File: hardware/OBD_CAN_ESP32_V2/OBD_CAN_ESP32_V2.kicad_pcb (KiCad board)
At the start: 2 copper layers, 66 x 36 mm, 20 parts, among them J3 ESP32_S3_DEVKITC_J1, J4 ESP32_S3_DEVKITC_J3, Q1 Q_PMOS_GDS, U1 SN65HVD230

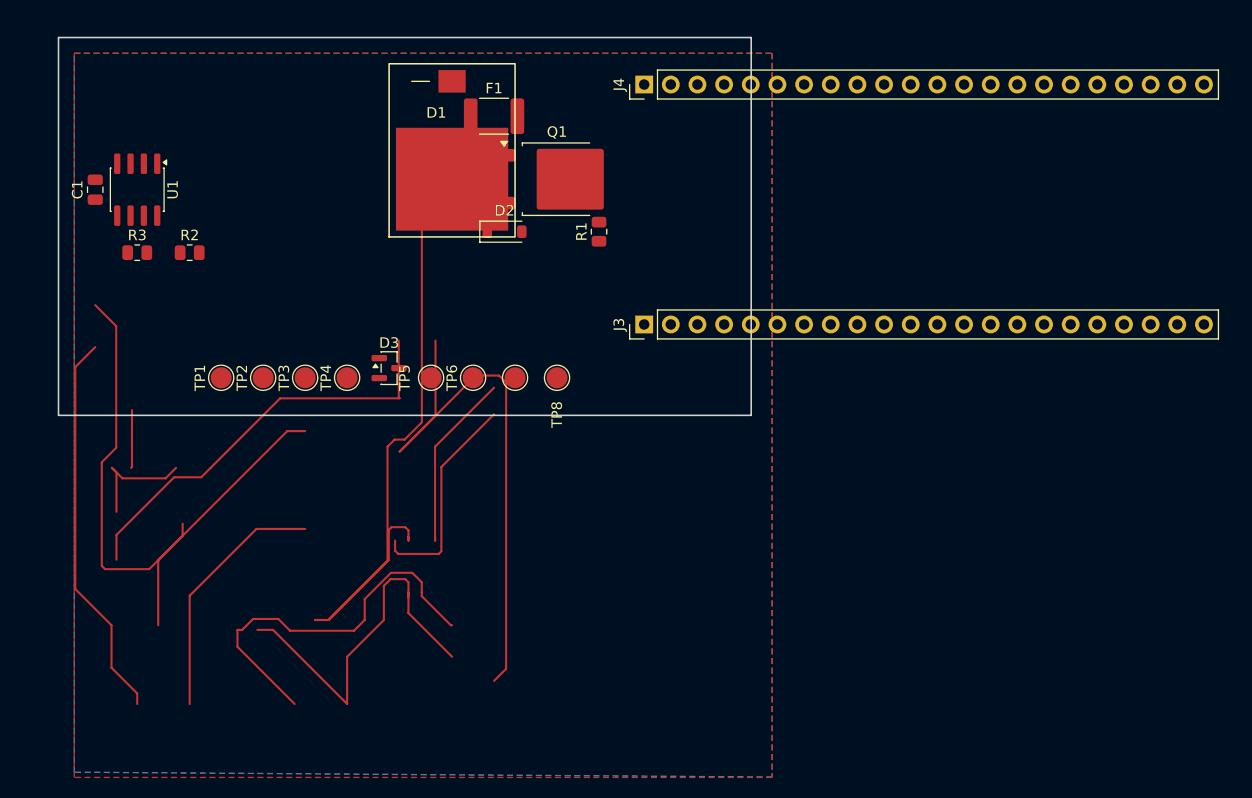
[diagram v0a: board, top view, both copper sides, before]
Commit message: hardware: V2 재작성 — 기존 라우팅/존 정리, 헤더 원점 수정
- V1의 트랙 97개 삭제(재배치로 무효), 구리 존 2개는 새 외곽으로 재정의
- 데브킷 헤더 원점을 좌측(61mm)으로 — 핀이 보드 안쪽으로 뻗도록
- 별도 폴더 OBD_CAN_ESP32_V2로 분리

Co-Authored-By: Claude Fable 5 <noreply@anthropic.com>
Claude-Session: https://claude.ai/code/session_015Lj2iN8K2AKiUuQKmtXaeP
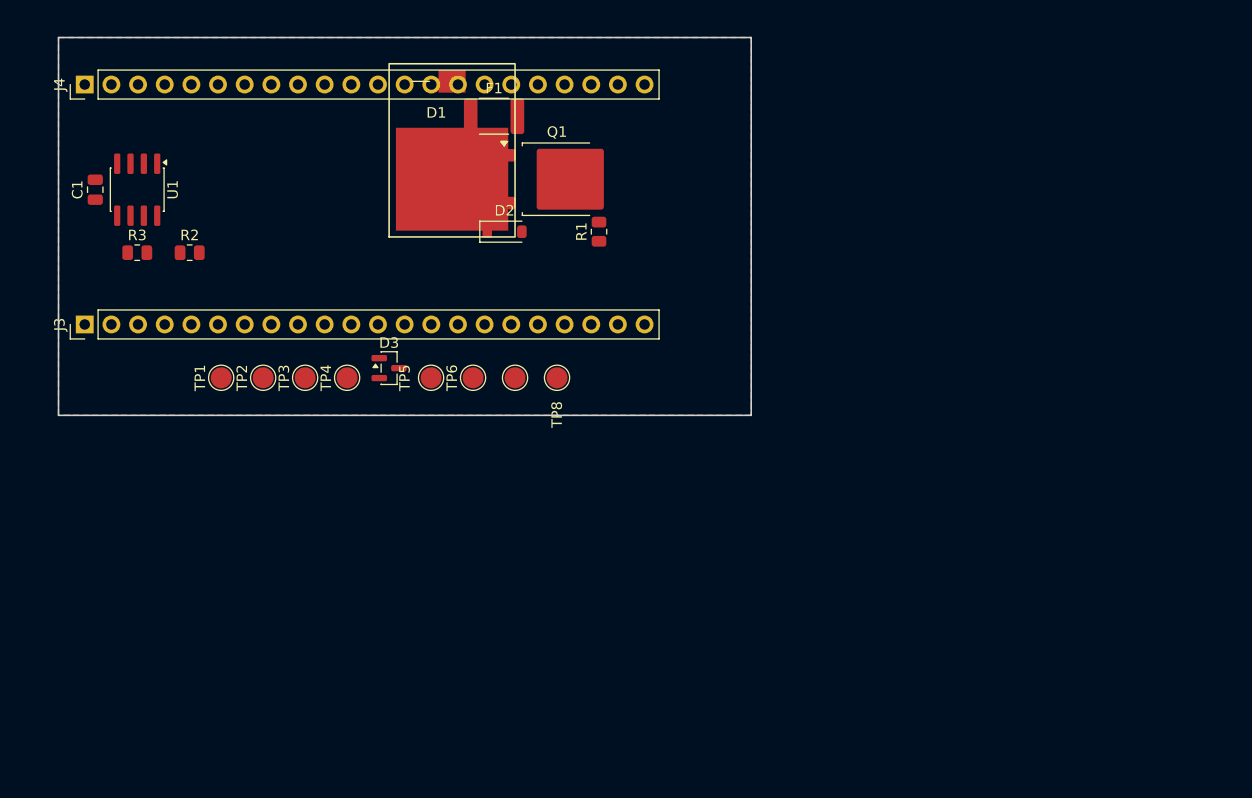
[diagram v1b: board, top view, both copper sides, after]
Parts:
- moved J3 53.3 mm to (61.0, 116.8)
- moved J4 53.3 mm to (61.0, 94.0)
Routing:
- net /+3V3: track 74.5 -> 0.00 mm
- net /VBAT_FUSED: track 61.8 -> 0.00 mm
- net /+5V: track 54.3 -> 0.00 mm
- net /VBAT_PROTECTED: track 40.3 -> 0.00 mm
- net /VBAT_OBD: track 37.2 -> 0.00 mm
- net /CAN_H: track 37.0 -> 0.00 mm
- net /CAN_L: track 36.2 -> 0.00 mm
- net /CHASSIS_GND: track 23.9 -> 0.00 mm
- net /CAN_RX: track 20.7 -> 0.00 mm
- net /CAN_TX: track 17.2 -> 0.00 mm
- net Net-(D2-K): track 11.3 -> 0.00 mm
- net /SIGNAL_GND: track 5.54 -> 0.00 mm

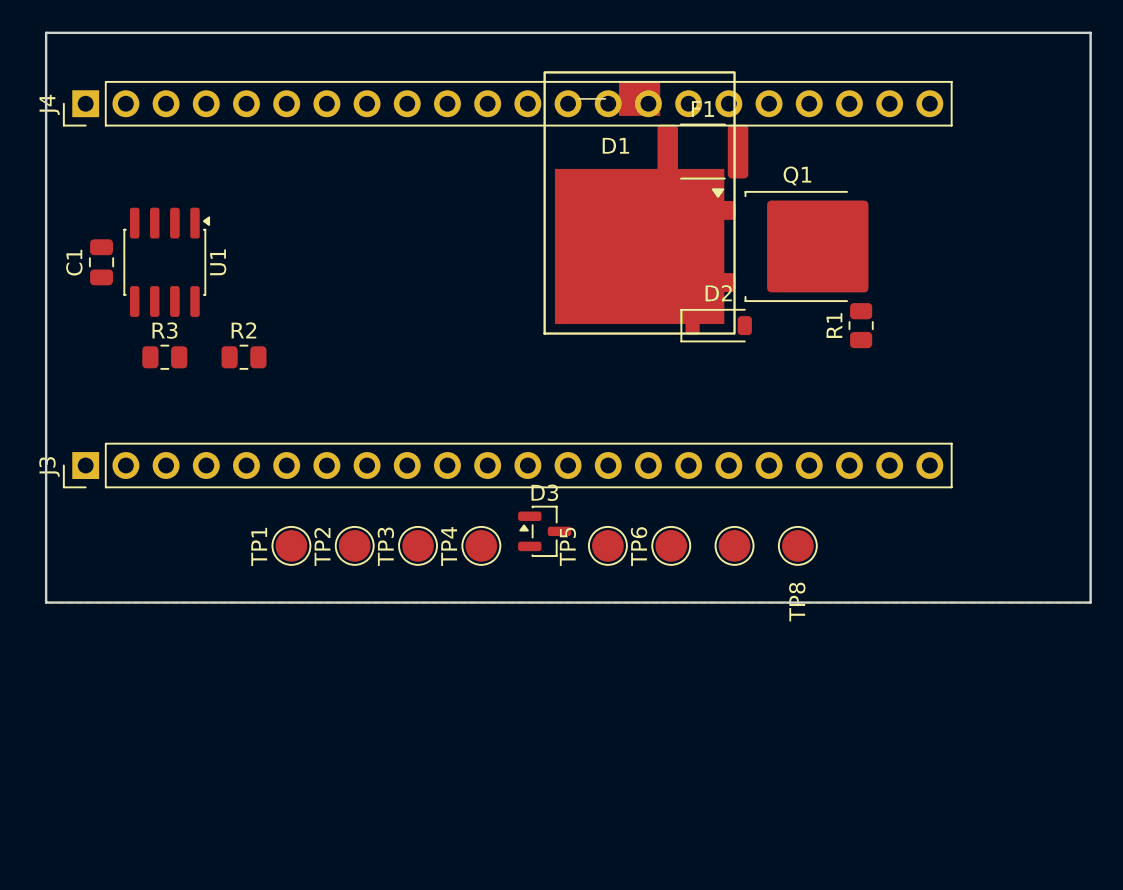
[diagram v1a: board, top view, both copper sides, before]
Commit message: hardware: V2 PCB 66x44 부품 배치 완료 (옵션2, 겹침 0 검증)
- 보드 66x36 → 66x44 (D1 SM8S24A 대형 TVS 수용)
- 존 배치: CAN(좌)/벅(중앙)/입력보호(하단)/커넥터+TP(최하단)
- 자체 커트야드 겹침 검사 통과 (겹침 0, 외곽 초과 0)

Co-Authored-By: Claude Fable 5 <noreply@anthropic.com>
Claude-Session: https://claude.ai/code/session_015Lj2iN8K2AKiUuQKmtXaeP
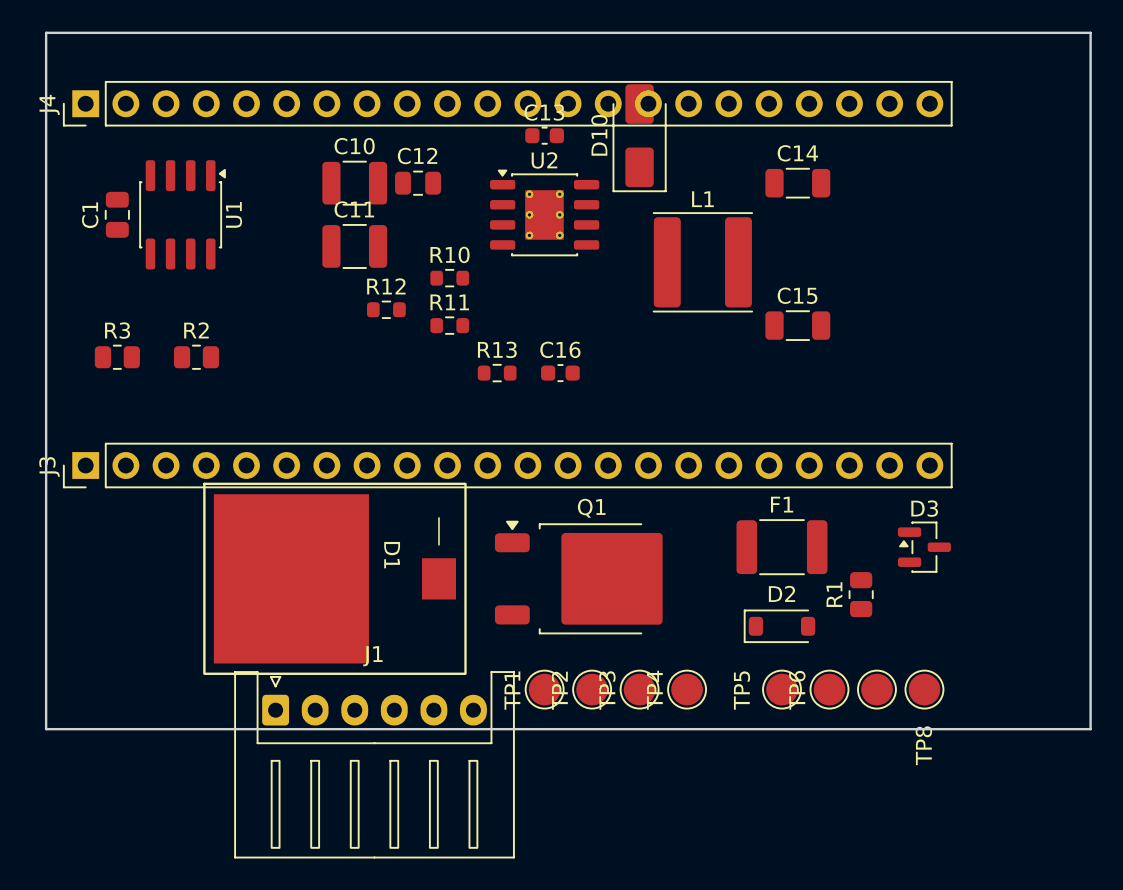
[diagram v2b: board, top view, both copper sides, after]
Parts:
- added C10: 2.2µF/100V, Capacitor_SMD:C_1210_3225Metric, F.Cu at (78.0, 99.0)
- added C11: 2.2µF/100V, Capacitor_SMD:C_1210_3225Metric, F.Cu at (78.0, 103.0)
- added C12: 100nF/100V, Capacitor_SMD:C_0805_2012Metric, F.Cu at (82.0, 99.0)
- added C13: 100nF, Capacitor_SMD:C_0603_1608Metric, F.Cu at (90.0, 96.0)
- added C14: 22µF/16V, Capacitor_SMD:C_1206_3216Metric, F.Cu at (106.0, 99.0)
- added C15: 22µF/16V, Capacitor_SMD:C_1206_3216Metric, F.Cu at (106.0, 108.0)
- added C16: 3300pF, Capacitor_SMD:C_0603_1608Metric, F.Cu at (91.0, 111.0)
- added D10: B360A, Diode_SMD:D_SMA, F.Cu at (96.0, 96.0)
- added J1: OBD-II INPUT, Connector_JST:JST_XH_S6B-XH-A_1x06_P2.50mm_Horizontal, F.Cu at (73.0, 132.3)
- added L1: 10µH 4A, Inductor_SMD:L_Sunlord_SWPA6045S, F.Cu at (100.0, 104.0)
- added R10: 52.3kΩ 1%, Resistor_SMD:R_0603_1608Metric, F.Cu at (84.0, 105.0)
- added R11: 10kΩ 1%, Resistor_SMD:R_0603_1608Metric, F.Cu at (84.0, 108.0)
- added R12: 182kΩ 1%, Resistor_SMD:R_0603_1608Metric, F.Cu at (80.0, 107.0)
- added R13: 8.06kΩ, Resistor_SMD:R_0603_1608Metric, F.Cu at (87.0, 111.0)
- added U2: TPS54360BDDA, Package_SO:HSOP-8-1EP_3.9x4.9mm_P1.27mm_EP2.41x3.1mm_ThermalVias, F.Cu at (90.0, 101.0)
- moved D1 30.4 mm to (74.0, 124.0), turned to 0 degrees
- moved F1 25.5 mm to (105.0, 122.0)
- moved Q1 24.7 mm to (93.0, 124.0)
- moved D3 24.0 mm to (114.0, 122.0)
- moved D2 19.4 mm to (105.0, 127.0)
- moved TP1 18.4 mm to (90.0, 131.0)
- moved TP2 17.5 mm to (93.0, 131.0)
- moved R1 17.0 mm to (110.0, 125.0)
- moved TP3 16.7 mm to (96.0, 131.0)
- moved TP4 15.9 mm to (99.0, 131.0)
- moved TP5 14.3 mm to (105.0, 131.0)
- moved TP6 13.5 mm to (108.0, 131.0)
- moved TP7 12.8 mm to (111.0, 131.0)
- moved TP8 12.1 mm to (114.0, 131.0)
- moved C1 3.16 mm to (63.0, 101.0)
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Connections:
- D2 pad 1: Net-(D2-K) -> /VBAT_PROTECTED
- D2 pad 2: /VBAT_PROTECTED -> Net-(D2-A)
- Q1 pad 1: Net-(D2-K) -> Net-(D2-A)
- R1 pad 1: Net-(D2-K) -> Net-(D2-A)
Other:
- board size 66 x 36 mm -> 66 x 44 mm

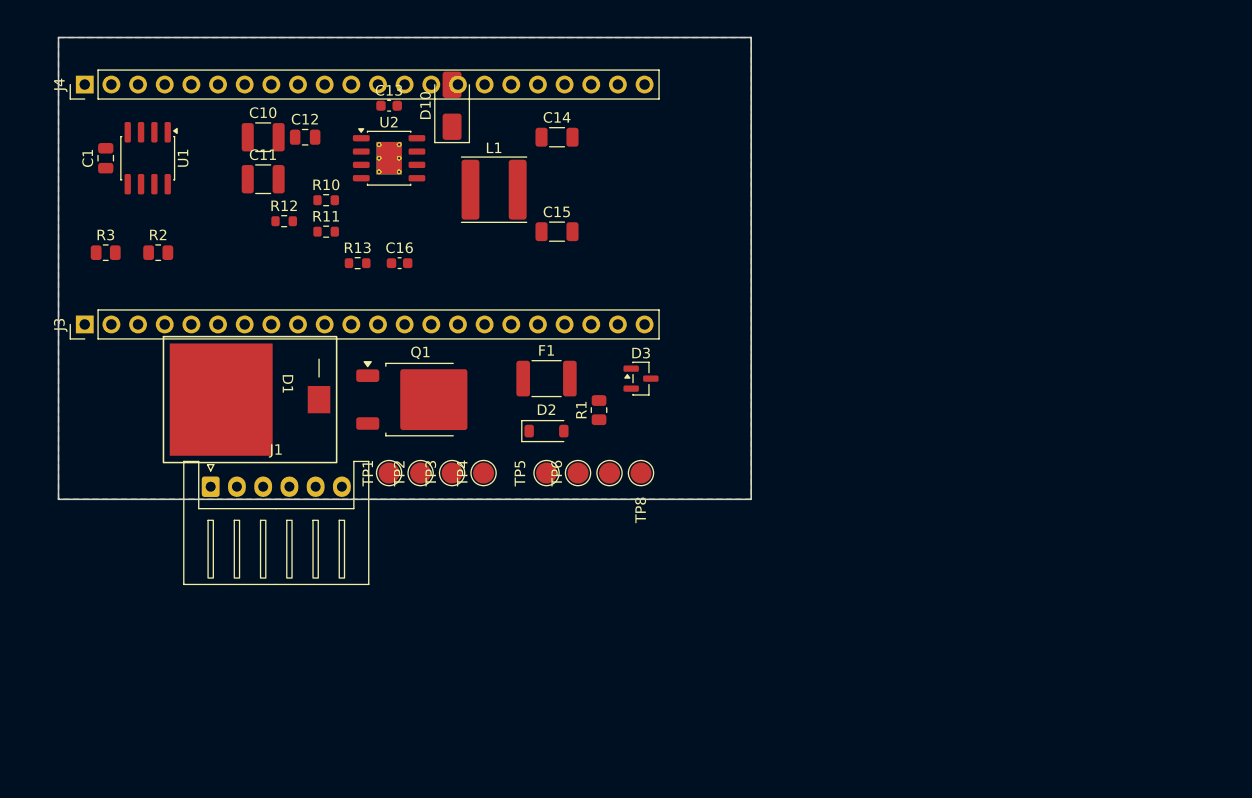
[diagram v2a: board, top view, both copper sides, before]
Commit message: hardware: V2 66x36 양면 배치 + M2.5 나사구멍 4개
- 보드 66x44 → 66x36 복원 (D1/Q1 뒷면 이설 전제)
- 앞면 부품 재배치, 겹침 0 검증
- 네 모서리 M2.5 마운팅홀(H1~H4) 추가 (케이스 고정용)
- D1/Q1은 뒷면 전환 대기 (사용자가 KiCad F키로 전환)

Co-Authored-By: Claude Fable 5 <noreply@anthropic.com>
Claude-Session: https://claude.ai/code/session_015Lj2iN8K2AKiUuQKmtXaeP
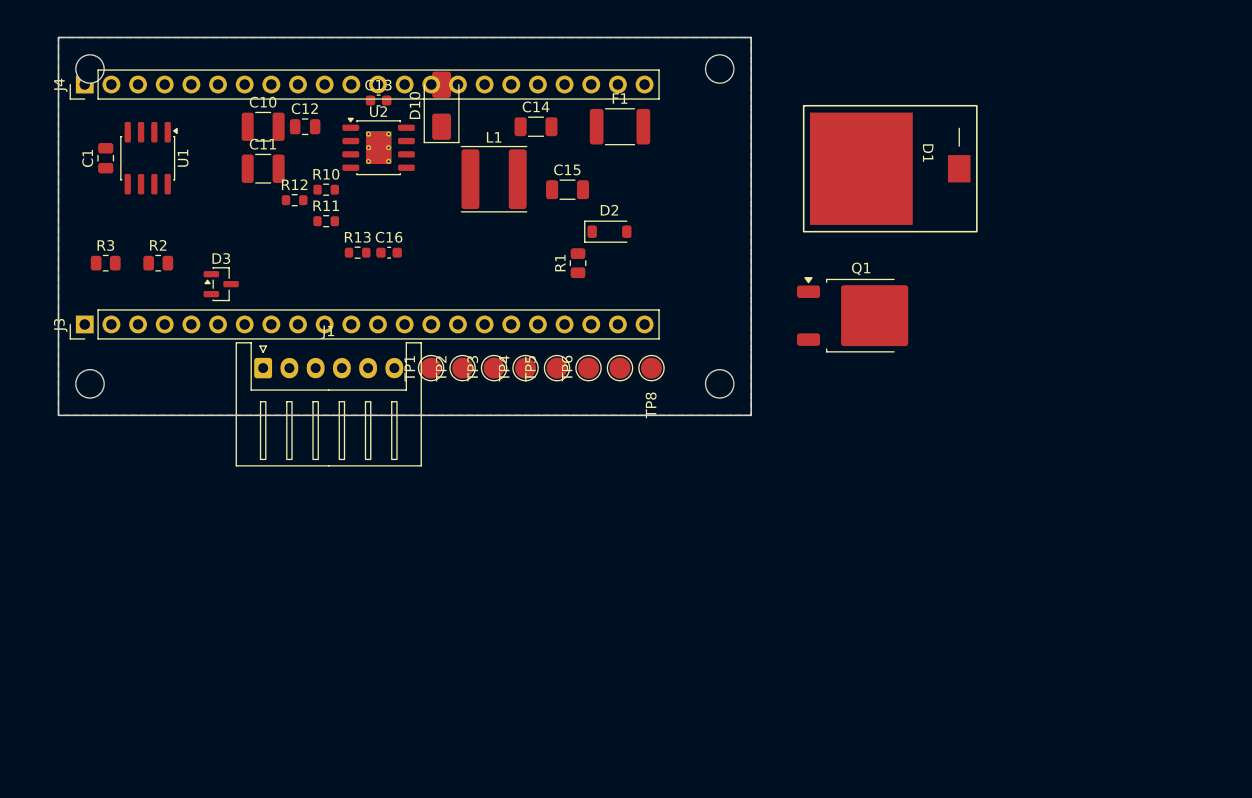
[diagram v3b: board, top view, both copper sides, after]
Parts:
- added H1: M2.5, MountingHole:MountingHole_2.7mm_M2.5, F.Cu at (61.5, 92.5)
- added H2: M2.5, MountingHole:MountingHole_2.7mm_M2.5, F.Cu at (121.5, 92.5)
- added H3: M2.5, MountingHole:MountingHole_2.7mm_M2.5, F.Cu at (61.5, 122.5)
- added H4: M2.5, MountingHole:MountingHole_2.7mm_M2.5, F.Cu at (121.5, 122.5)
- moved D1 64.8 mm to (135.0, 102.0)
- moved Q1 42.8 mm to (135.0, 116.0)
- moved D3 41.0 mm to (74.0, 113.0)
- moved F1 25.0 mm to (112.0, 98.0)
- moved D2 19.9 mm to (111.0, 108.0)
- moved R1 14.1 mm to (108.0, 111.0)
- moved J1 12.4 mm to (78.0, 121.0)
- moved TP1 10.8 mm to (94.0, 121.0)
- moved TP2 10.8 mm to (97.0, 121.0)
- moved TP3 10.8 mm to (100.0, 121.0)
- moved TP4 10.8 mm to (103.0, 121.0)
- moved TP5 10.0 mm to (106.0, 121.0)
- moved TP6 10.0 mm to (109.0, 121.0)
- moved TP7 10.0 mm to (112.0, 121.0)
- moved TP8 10.0 mm to (115.0, 121.0)
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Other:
- board size 66 x 44 mm -> 66 x 36 mm

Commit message: hardware: V2 최소화 61.5x30 (TP·OBD커넥터도 뒷면 이설 전제)
- 보드 66x36 → 61.5x30 (데브킷 그림자 수준, 면적 -22%)
- 앞면=소형 SMD만, 뒷면 이설 대기: D1/Q1/J1/TP1~8
- M2.5 나사구멍 4개 재배치(헤더 핀 간섭 없이 코너)
- 겹침 0 검증

Co-Authored-By: Claude Fable 5 <noreply@anthropic.com>
Claude-Session: https://claude.ai/code/session_015Lj2iN8K2AKiUuQKmtXaeP
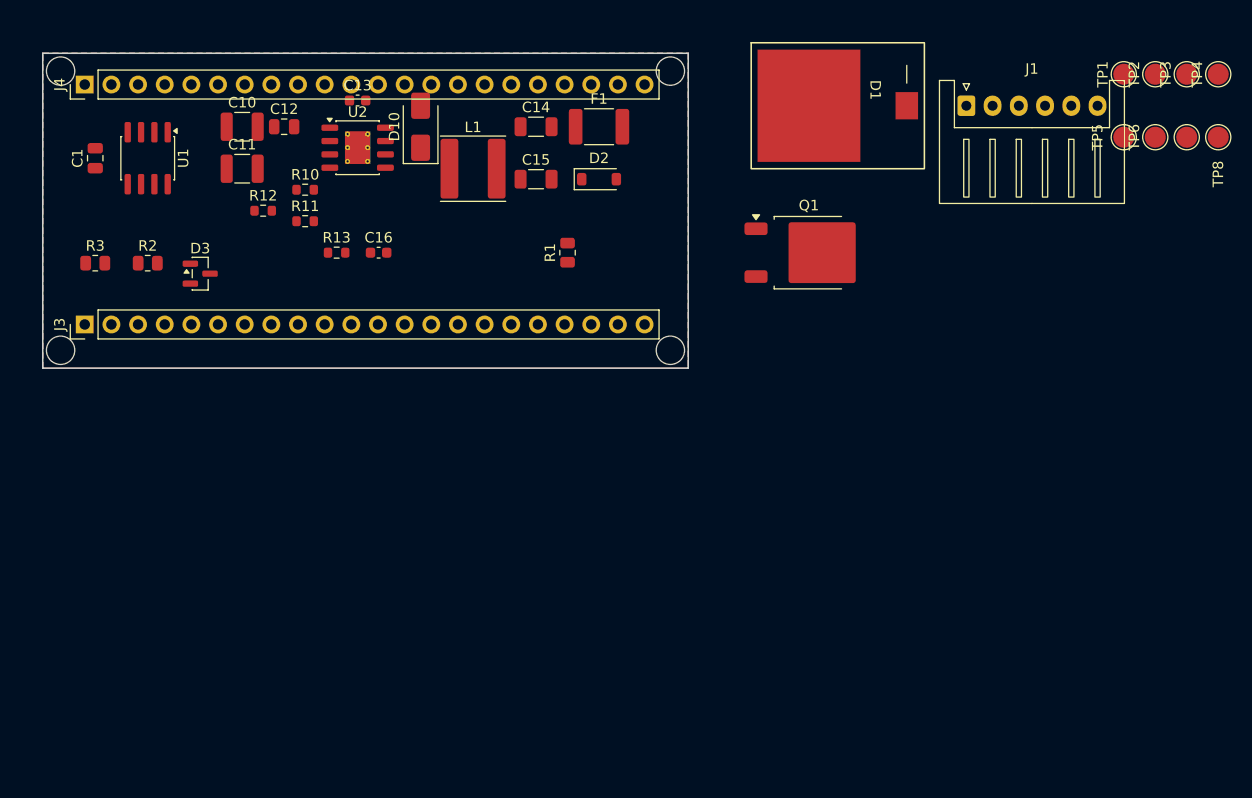
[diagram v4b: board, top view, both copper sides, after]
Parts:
- moved TP1 71.7 mm to (160.0, 93.0)
- moved TP2 71.7 mm to (163.0, 93.0)
- moved TP3 71.7 mm to (166.0, 93.0)
- moved TP4 71.7 mm to (169.0, 93.0)
- moved J1 71.5 mm to (145.0, 96.0)
- moved TP5 58.3 mm to (160.0, 99.0)
- moved TP6 58.3 mm to (163.0, 99.0)
- moved TP7 58.3 mm to (166.0, 99.0)
- moved TP8 58.3 mm to (169.0, 99.0)
- moved D1 7.81 mm to (130.0, 96.0)
- moved Q1 7.81 mm to (130.0, 110.0)
- moved H4 5.69 mm to (116.8, 119.3)
- moved D2 5.10 mm to (110.0, 103.0)
- moved H2 4.70 mm to (116.8, 92.7)
- moved H3 4.25 mm to (58.7, 119.3)
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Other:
- board size 66 x 36 mm -> 61.5 x 30 mm
